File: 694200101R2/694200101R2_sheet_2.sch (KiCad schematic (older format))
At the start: 89 parts, among them U4 M24512-DFMN6TP, U5 IS31FL3733B-QFLS4-TR, U6 IS31FL3733B-QFLS4-TR

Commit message: created rev2 to work
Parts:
- renumbered C26 to C?, C27 to C?, C11 to C?, C12 to C?, C13 to C?, C14 to C?, C15 to C?, C16 to C?, C24 to C?, C23 to C?, C22 to C?, C21 to C?, C20 to C?, C19 to C?, C17 to C?, C18 to C?, R16 to R?, R15 to R?, R17 to R?, R19 to R?, R18 to R?, R20 to R?, U4 to U?, U5 to U?, U6 to U?

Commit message: adjusted led and added pull on program
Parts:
- gave numbers to parts that had none: 25

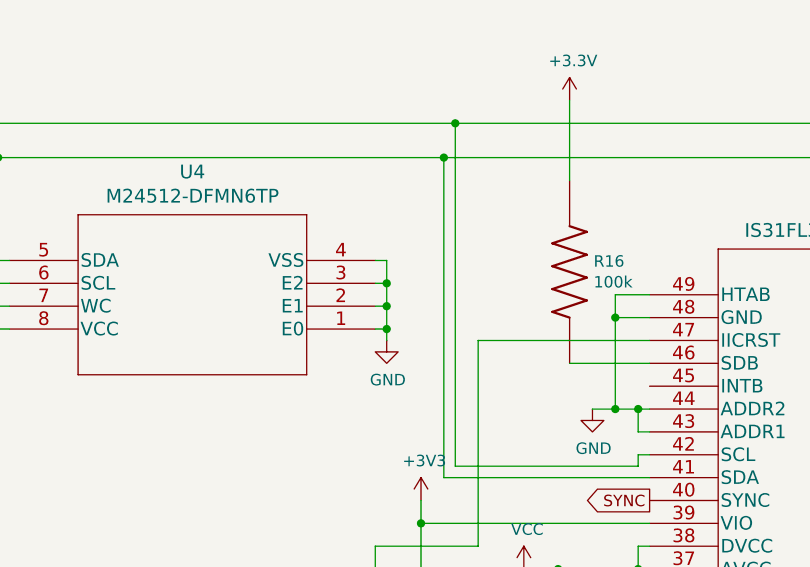
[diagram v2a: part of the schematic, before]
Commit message: updated eeprom address
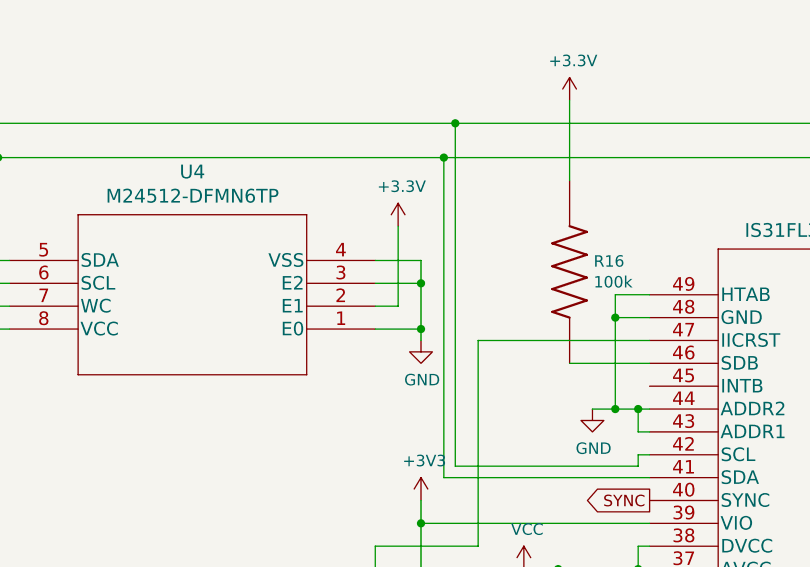
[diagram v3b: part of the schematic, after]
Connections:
- net +3V3: now also U4.2 (E1)
- net GND: no longer U4.2 (E1)
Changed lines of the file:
@@
 Wire Wire Line
 	13100 6900 13100 6800
-$Comp
-L STM_EEPROM:M24512-DFMN6TP U4
-U 1 1 60F1F6EF
-P 2800 7900
-F 0 "U4" H 3600 7213 60  0000 C CNN
-F 1 "M24512-DFMN6TP" H 3600 7319 60  0000 C CNN
-F 2 "STM:STMicroelectronics-SO8N-SO-A-0-2-MFG" H 3600 8140 60  0001 C CNN
-F 3 "" H 2800 7900 60  0000 C CNN
-	1    2800 7900
-	-1   0    0    1
-$EndComp
 Wire Wire Line
 	1050 7000 1100 7000
@@
 	1150 7150 3100 7150
 Wire Wire Line
-	2800 7600 2850 7600
+	3000 7600 3000 7700
+Connection ~ 3000 7700
+Connection ~ 3000 7900
 Wire Wire Line
-	2850 7600 2850 7700
-Wire Wire Line
-	2800 7700 2850 7700
-Connection ~ 2850 7700
-Wire Wire Line
-	2850 7700 2850 7800
-Wire Wire Line
-	2800 7800 2850 7800
-Connection ~ 2850 7800
-Wire Wire Line
-	2850 7800 2850 7900
-Wire Wire Line
-	2800 7900 2850 7900
-Connection ~ 2850 7900
-Wire Wire Line
-	2850 7900 2850 7950
+	3000 7900 3000 7950
 Wire Wire Line
 	1200 7800 1050 7800
@@
 Wire Wire Line
 	950  7900 950  7850
-$Comp
-L power:GND #PWR019
-U 1 1 61F36928
-P 2850 7950
-F 0 "#PWR019" H 2850 7700 50  0001 C CNN
-F 1 "GND" H 2855 7777 50  0000 C CNN
-F 2 "" H 2850 7950 50  0001 C CNN
-F 3 "" H 2850 7950 50  0001 C CNN
-	1    2850 7950
-	1    0    0    -1
-$EndComp
 $Sheet
 S 15250 4300 950  700
@@
 F1 "694200101R2_sheet_3.sch" 50
 $EndSheet
+Wire Wire Line
+	3000 7700 3000 7900
+$Comp
+L STM_EEPROM:M24512-DFMN6TP U4
+U 1 1 60F1F6EF
+P 2800 7900
+F 0 "U4" H 3600 7213 60  0000 C CNN
+F 1 "M24512-DFMN6TP" H 3600 7319 60  0000 C CNN
+F 2 "STM:STMicroelectronics-SO8N-SO-A-0-2-MFG" H 3600 8140 60  0001 C CNN
+F 3 "" H 2800 7900 60  0000 C CNN
+	1    2800 7900
+	-1   0    0    1
+$EndComp
+$Comp
+L power:GND #PWR019
+U 1 1 61F36928
+P 3000 7950
+F 0 "#PWR019" H 3000 7700 50  0001 C CNN
+F 1 "GND" H 3005 7777 50  0000 C CNN
+F 2 "" H 3000 7950 50  0001 C CNN
+F 3 "" H 3000 7950 50  0001 C CNN
+	1    3000 7950
+	1    0    0    -1
+$EndComp
+Wire Wire Line
+	2800 7900 3000 7900
+Wire Wire Line
+	2800 7700 3000 7700
+Wire Wire Line
+	2800 7600 3000 7600
+$Comp
+L power:+3.3V #PWR?
+U 1 1 637E67B4
+P 2900 7450
+F 0 "#PWR?" H 2900 7300 50  0001 C CNN
+F 1 "+3.3V" H 2915 7623 50  0000 C CNN
+F 2 "" H 2900 7450 50  0001 C CNN
+F 3 "" H 2900 7450 50  0001 C CNN
+	1    2900 7450
+	1    0    0    -1
+$EndComp
+Wire Wire Line
+	2900 7800 2900 7450
+Wire Wire Line
+	2800 7800 2900 7800
 $EndSCHEMATC

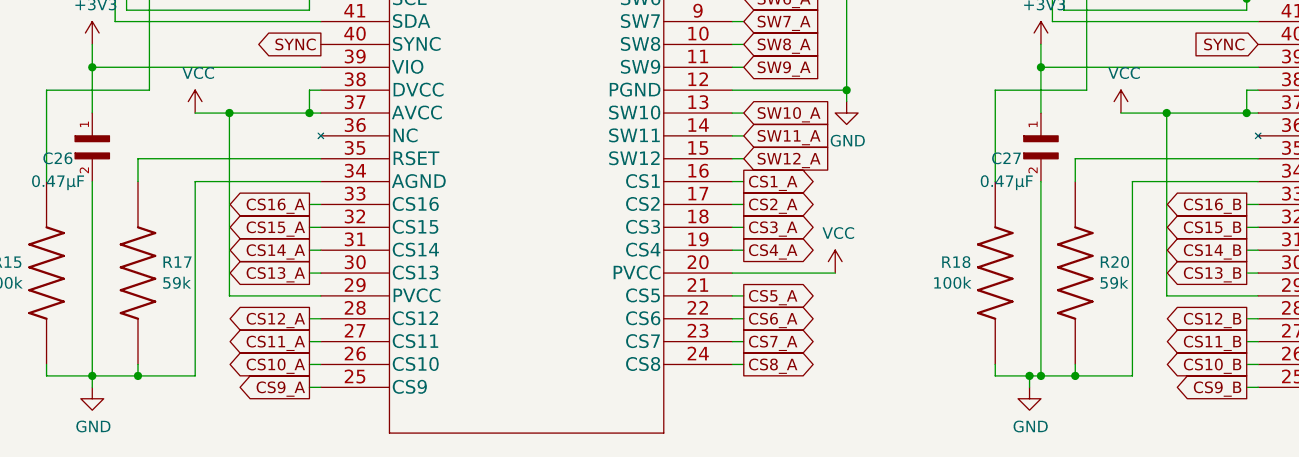
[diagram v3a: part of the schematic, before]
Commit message: Updated LED driver footprint
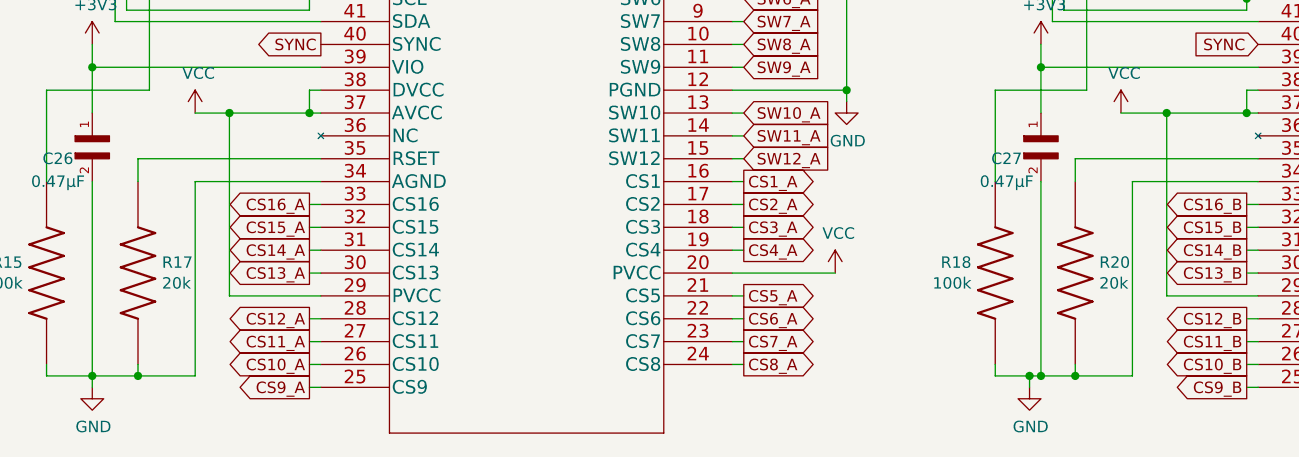
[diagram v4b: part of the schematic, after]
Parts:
- R17, R20: resistance 59k -> 20k
- U5, U6: footprint cldg:QFN-48_EP_6.6x6.6_Pitch0.4mm -> Package_QFP:TQFP-48-1EP_7x7mm_P0.5mm_EP5x5mm
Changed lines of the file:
@@
 F 0 "U5" H 6700 8137 60  0000 C CNN
 F 1 "IS31FL3733B-QFLS4-TR" H 6700 8031 60  0000 C CNN
-F 2 "cldg:QFN-48_EP_6.6x6.6_Pitch0.4mm" H 6700 7990 60  0001 C CNN
+F 2 "Package_QFP:TQFP-48-1EP_7x7mm_P0.5mm_EP5x5mm" H 6700 7990 60  0001 C CNN
 F 3 "" H 5800 7750 60  0000 C CNN
 	1    5800 7750
@@
 F 2 "Resistor-Libs:RESC6332X70N" H 3200 9650 50  0001 L BNN
 F 3 "" H 3200 9650 50  0001 L BNN
-F 4 "59k" V 3245 9755 50  0000 L CNN "resistance"
+F 4 "20k" V 3245 9755 50  0000 L CNN "resistance"
 	1    3200 9650
 	0    1    1    0
@@
 F 0 "U6" H 10800 8137 60  0000 C CNN
 F 1 "IS31FL3733B-QFLS4-TR" H 10800 8031 60  0000 C CNN
-F 2 "cldg:QFN-48_EP_6.6x6.6_Pitch0.4mm" H 10800 7990 60  0001 C CNN
+F 2 "Package_QFP:TQFP-48-1EP_7x7mm_P0.5mm_EP5x5mm" H 10800 7990 60  0001 C CNN
 F 3 "" H 9900 7750 60  0000 C CNN
 	1    9900 7750
@@
 F 2 "Resistor-Libs:RESC6332X70N" H 7300 9650 50  0001 L BNN
 F 3 "" H 7300 9650 50  0001 L BNN
-F 4 "59k" V 7345 9755 50  0000 L CNN "resistance"
+F 4 "20k" V 7345 9755 50  0000 L CNN "resistance"
 	1    7300 9650
 	0    1    1    0
@@
 	2800 7600 3000 7600
 $Comp
-L power:+3.3V #PWR?
+L power:+3.3V #PWR0112
 U 1 1 637E67B4
 P 2900 7450
-F 0 "#PWR?" H 2900 7300 50  0001 C CNN
+F 0 "#PWR0112" H 2900 7300 50  0001 C CNN
 F 1 "+3.3V" H 2915 7623 50  0000 C CNN
 F 2 "" H 2900 7450 50  0001 C CNN

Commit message: Prettied up schematic
Updated Schematic to be more readable and not as crazily wired
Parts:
- U5, U6: footprint Package_QFP:TQFP-48-1EP_7x7mm_P0.5mm_EP5x5mm -> Package_QFP:TQFP-48-1EP_7x7mm_P0.5mm_EP5x5mm_ThermalVias
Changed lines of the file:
@@
 F 0 "U5" H 6700 8137 60  0000 C CNN
 F 1 "IS31FL3733B-QFLS4-TR" H 6700 8031 60  0000 C CNN
-F 2 "Package_QFP:TQFP-48-1EP_7x7mm_P0.5mm_EP5x5mm" H 6700 7990 60  0001 C CNN
+F 2 "Package_QFP:TQFP-48-1EP_7x7mm_P0.5mm_EP5x5mm_ThermalVias" H 6700 7990 60  0001 C CNN
 F 3 "" H 5800 7750 60  0000 C CNN
 	1    5800 7750
@@
 F 0 "U6" H 10800 8137 60  0000 C CNN
 F 1 "IS31FL3733B-QFLS4-TR" H 10800 8031 60  0000 C CNN
-F 2 "Package_QFP:TQFP-48-1EP_7x7mm_P0.5mm_EP5x5mm" H 10800 7990 60  0001 C CNN
+F 2 "Package_QFP:TQFP-48-1EP_7x7mm_P0.5mm_EP5x5mm_ThermalVias" H 10800 7990 60  0001 C CNN
 F 3 "" H 9900 7750 60  0000 C CNN
 	1    9900 7750

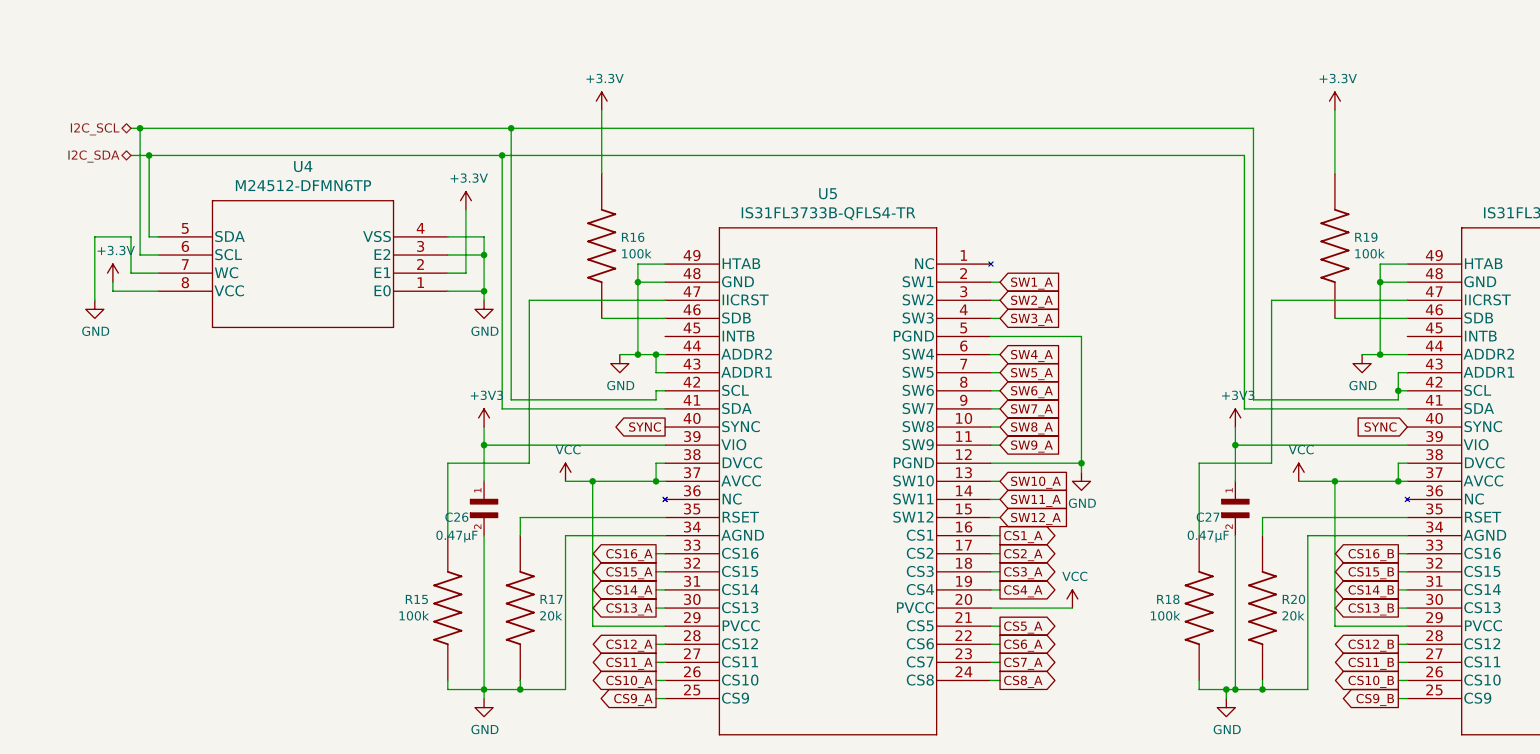
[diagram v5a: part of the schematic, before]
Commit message: Updated Footprints and Fixed Schematic Warnings
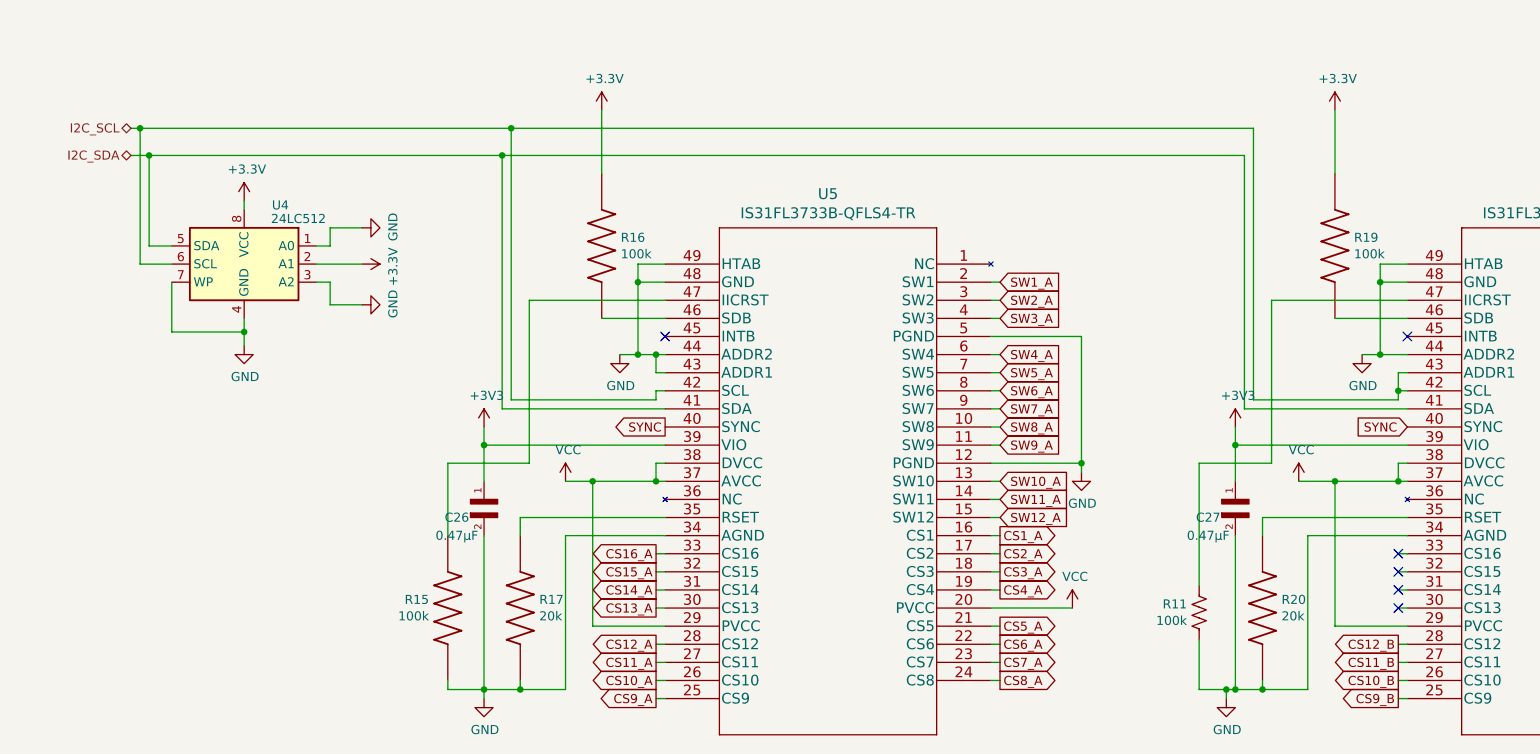
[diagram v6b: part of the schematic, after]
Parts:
- removed R18: RMCF0603FT100K, Resistor-Libs:RESC1508X55N, symbol Resistor-Lib:RMCF0603FT100K
- removed U4: M24512-DFMN6TP, STM:STMicroelectronics-SO8N-SO-A-0-2-MFG, symbol STM_EEPROM:M24512-DFMN6TP
- removed U5, U6: IS31FL3733B-QFLS4-TR, Package_QFP:TQFP-48-1EP_7x7mm_P0.5mm_EP5x5mm_ThermalVias, symbol Lumissil:IS31FL3733B-QFLS4-TR
- added R11: 100k, Resistor_SMD:R_0603_1608Metric, symbol Device:R_US
- added U4: 24LC512, Package_SO:SO-8_3.9x4.9mm_P1.27mm, symbol Memory_EEPROM:24LC512
- added U5, U6: IS31FL3733B-QFLS4-TR, Package_QFP:TQFP-48-1EP_7x7mm_P0.5mm_EP5x5mm_ThermalVias, symbol cldg:IS31FL3733B-QFLS4-TR
- C11, C13, C15, C20, C22, C24, C26, C27: footprint capacitor-lib:CAPC1608X90N -> Capacitor_SMD:C_0603_1608Metric
- C12, C14, C16, C19, C21, C23: footprint capacitor-lib:Samsung-CL10-09_2006-0-IPC_C -> Capacitor_SMD:C_0603_1608Metric
- R15, R16, R19: footprint Resistor-Libs:RESC1508X55N -> Resistor_SMD:R_0603_1608Metric
- R17, R20: footprint Resistor-Libs:RESC6332X70N -> Resistor_SMD:R_2512_6332Metric
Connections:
- net +3V3: now also U4.2 (A1), U4.8 (VCC), U5.39 (VIO), U6.39 (VIO)
- net CS10_A: now also U5.26 (CS10)
- net CS10_B: now also U6.26 (CS10)
- net CS11_A: now also U5.27 (CS11)
- net CS11_B: now also U6.27 (CS11)
- net CS12_A: now also U5.28 (CS12)
- net CS12_B: now also U6.28 (CS12)
- net CS13_A: now also U5.30 (CS13)
- net CS14_A: now also U5.31 (CS14)
- net CS15_A: now also U5.32 (CS15)
- net CS16_A: now also U5.33 (CS16)
- net CS1_A: now also U5.16 (CS1)
- net CS1_B: now also U6.16 (CS1)
- net CS2_A: now also U5.17 (CS2)
- net CS2_B: now also U6.17 (CS2)
- net CS3_A: now also U5.18 (CS3)
- net CS3_B: now also U6.18 (CS3)
- net CS4_A: now also U5.19 (CS4)
- net CS4_B: now also U6.19 (CS4)
- net CS5_A: now also U5.21 (CS5)
- net CS5_B: now also U6.21 (CS5)
- net CS6_A: now also U5.22 (CS6)
- net CS6_B: now also U6.22 (CS6)
- net CS7_A: now also U5.23 (CS7)
- net CS7_B: now also U6.23 (CS7)
- net CS8_A: now also U5.24 (CS8)
- net CS8_B: now also U6.24 (CS8)
- net CS9_A: now also U5.25 (CS9)
- net CS9_B: now also U6.25 (CS9)
- net GND: now also R11.2, U4.1 (A0), U4.3 (A2), U4.4 (GND), U4.7 (WP), U5.12 (PGND), U5.34 (AGND), U5.43 (ADDR1), U5.44 (ADDR2), U5.48 (GND), U5.49 (HTAB), U5.5 (PGND), U6.12 (PGND), U6.34 (AGND), U6.44 (ADDR2), U6.48 (GND), U6.49 (HTAB), U6.5 (PGND)
- net I2C_SCL: now also U4.6 (SCL), U5.42 (SCL), U6.42 (SCL), U6.43 (ADDR1)
- net I2C_SDA: now also U4.5 (SDA), U5.41 (SDA), U6.41 (SDA)
- net SW10_A: now also U5.13 (SW10)
- net SW10_B: now also U6.13 (SW10)
- net SW11_A: now also U5.14 (SW11)
- net SW11_B: now also U6.14 (SW11)
- net SW12_A: now also U5.15 (SW12)
- net SW12_B: now also U6.15 (SW12)
- net SW1_A: now also U5.2 (SW1)
- net SW1_B: now also U6.2 (SW1)
- net SW2_A: now also U5.3 (SW2)
- net SW2_B: now also U6.3 (SW2)
- net SW3_A: now also U5.4 (SW3)
- net SW3_B: now also U6.4 (SW3)
- net SW4_A: now also U5.6 (SW4)
- net SW4_B: now also U6.6 (SW4)
- net SW5_A: now also U5.7 (SW5)
- net SW5_B: now also U6.7 (SW5)
- net SW6_A: now also U5.8 (SW6)
- net SW6_B: now also U6.8 (SW6)
- net SW7_A: now also U5.9 (SW7)
- net SW7_B: now also U6.9 (SW7)
- net SW8_A: now also U5.10 (SW8)
- net SW8_B: now also U6.10 (SW8)
- net SW9_A: now also U5.11 (SW9)
- net SW9_B: now also U6.11 (SW9)
- net SYNC: now also U5.40 (SYNC), U6.40 (SYNC)
- net VCC: now also U5.20 (PVCC), U5.29 (PVCC), U5.37 (AVCC), U5.38 (DVCC), U6.20 (PVCC), U6.29 (PVCC), U6.37 (AVCC), U6.38 (DVCC)
- net at R17.1: now also U5.35 (RSET)
- net at R16.2: now also U5.46 (SDB)
- net at R15.1: now also U5.47 (IICRST)
- net at R20.1: now also U6.35 (RSET)
- net at R19.2: now also U6.46 (SDB)
- new net: R11.1, U6.47 (IICRST)
- no-connect marks 0 -> 6

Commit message: Updated Schematic to use KiCad LED Driver Symbols
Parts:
- removed C11, C13, C15, C20, C22, C24, C26, C27: CL10B474KA8NFNC, Capacitor_SMD:C_0603_1608Metric, symbol capacitor-lib:CL10B474KA8NFNC
- removed C12, C14, C16, C19, C21, C23: CL10B104KB8NNNL, Capacitor_SMD:C_0603_1608Metric, symbol capacitor-lib:CL10B104KB8NNNL
- removed C17, C18: TAJB226K016RNJ, capacitor-lib:CAPPC3528X210N, symbol capacitor-lib:TAJB226K016RNJ
- removed R11: 100k, Resistor_SMD:R_0603_1608Metric, symbol Device:R_US
- removed R15, R16, R19: RMCF0603FT100K, Resistor_SMD:R_0603_1608Metric, symbol Resistor-Lib:RMCF0603FT100K
- removed R17, R20: RMCF2512FT59K0, Resistor_SMD:R_2512_6332Metric, symbol Resistor-Lib:RMCF2512FT20K0
- removed U4: 24LC512, Package_SO:SO-8_3.9x4.9mm_P1.27mm, symbol Memory_EEPROM:24LC512
- removed U5, U6: IS31FL3733B-QFLS4-TR, Package_QFP:TQFP-48-1EP_7x7mm_P0.5mm_EP5x5mm_ThermalVias, symbol cldg:IS31FL3733B-QFLS4-TR
- added C11, C13, C15, C26: 0.47uF, Capacitor_SMD:C_0603_1608Metric, symbol Device:C
- added C12, C14, C16: 100nF, Capacitor_SMD:C_0603_1608Metric, symbol Device:C
- added C17: 22uF, capacitor-lib:CAPPC3528X210N, symbol Device:CP1
- added R12, R13: 100k, Resistor_SMD:R_0603_1608Metric, symbol Device:R_US
- added R14: 59k, Resistor_SMD:R_2512_6332Metric, symbol Device:R_US
- added U5: IS31FL3733-TQ, Package_QFP:TQFP-48-1EP_7x7mm_P0.5mm_EP5x5mm_ThermalVias, symbol cldg:IS31FL3733-TQ
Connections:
- net +3V3: now also C26.1, R13.2, U5.39 (VIO)
- net CS10_A: now also U5.26 (CS10)
- net CS11_A: now also U5.27 (CS11)
- net CS12_A: now also U5.28 (CS12)
- net CS13_A: now also U5.30 (CS13)
- net CS14_A: now also U5.31 (CS14)
- net CS15_A: now also U5.32 (CS15)
- net CS16_A: now also U5.33 (CS16)
- net CS1_A: now also U5.16 (CS1)
- net CS2_A: now also U5.17 (CS2)
- net CS3_A: now also U5.18 (CS3)
- net CS4_A: now also U5.19 (CS4)
- net CS5_A: now also U5.21 (CS5)
- net CS6_A: now also U5.22 (CS6)
- net CS7_A: now also U5.23 (CS7)
- net CS8_A: now also U5.24 (CS8)
- net CS9_A: now also U5.25 (CS9)
- net GND: now also C11.2, C12.2, C13.2, C14.2, C15.2, C16.2, C17.2, C26.2, R12.1, R14.2, U5.12 (PGND), U5.34 (AGND), U5.43 (ADDR1), U5.44 (ADDR2), U5.48 (GND), U5.49 (GND), U5.5 (PGND)
- net I2C_SCL: now also U5.42 (SCL)
- net I2C_SDA: now also U5.41 (SDA)
- net SW10_A: now also U5.13 (SW10)
- net SW11_A: now also U5.14 (SW11)
- net SW12_A: now also U5.15 (SW12)
- net SW1_A: now also U5.2 (SW1)
- net SW2_A: now also U5.3 (SW2)
- net SW3_A: now also U5.4 (SW3)
- net SW4_A: now also U5.6 (SW4)
- net SW5_A: now also U5.7 (SW5)
- net SW6_A: now also U5.8 (SW6)
- net SW7_A: now also U5.9 (SW7)
- net SW8_A: now also U5.10 (SW8)
- net SW9_A: now also U5.11 (SW9)
- net VCC: now also C11.1, C12.1, C13.1, C14.1, C15.1, C16.1, C17.1, U5.20 (PVCC), U5.29 (PVCC), U5.37 (AVCC), U5.38 (DVCC)
- new net: R12.2, U5.47 (IICRST)
- new net: R13.1, U5.46 (~SDB)
- new net: R14.1, U5.35 (RSET)
- new net SYNC_OUT: U5.40 (SYNC)
- no-connect marks 6 -> 1
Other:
- note added: "LED Driver A - Addr"
- note added: "LED Driver A - Power Filtering"
- note removed: "LED_DRIVER_B\nP20"
- note removed: "LED_DRIVER_B\nP29"
- note removed: "LED_DRIVER_B\nP37/38"
- note removed: "LED_DRIVER_B\nPWR_FILTER"

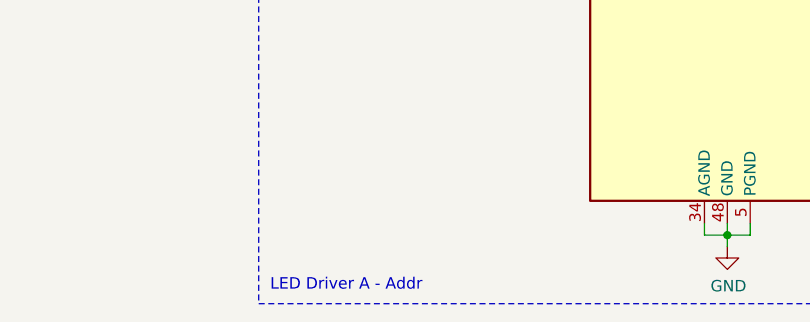
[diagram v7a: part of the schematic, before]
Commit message: Updated Address in schematic
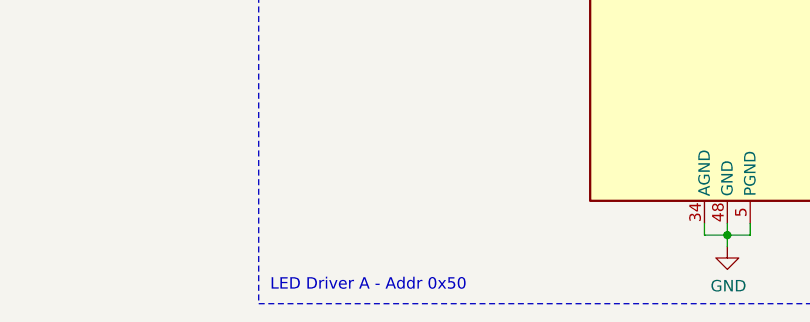
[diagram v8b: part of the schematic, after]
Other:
- note added: "LED Driver A - Addr 0x50"
- note removed: "LED Driver A - Addr"
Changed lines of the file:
@@
 	5350 5750 5350 10200
 Text Notes 5400 10150 0    50   ~ 0
-LED Driver A - Addr
+LED Driver A - Addr 0x50
 Wire Notes Line
 	11425 5750 11425 10200
